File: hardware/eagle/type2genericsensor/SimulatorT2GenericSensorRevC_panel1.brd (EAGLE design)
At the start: 48.3 x 48.3 mm, 13 parts

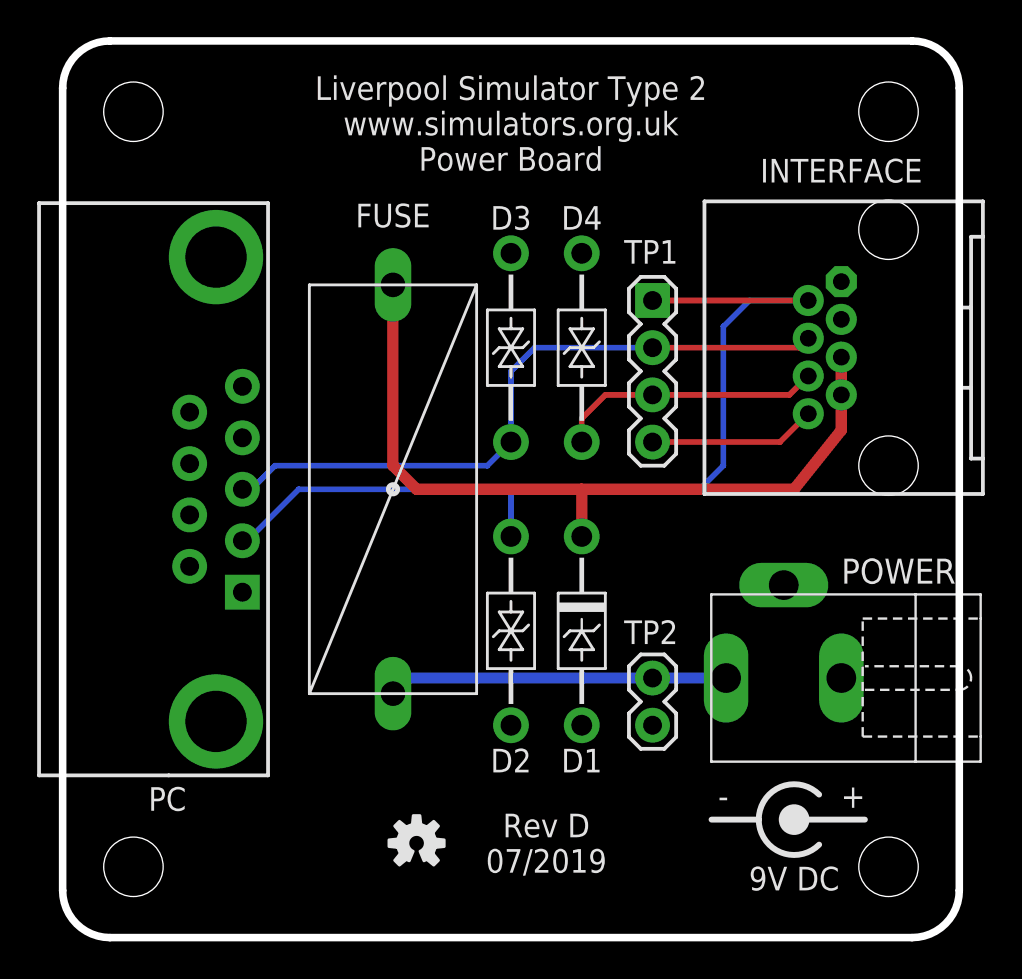
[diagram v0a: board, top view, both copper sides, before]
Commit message: Board Housekeeping
URL on silkscreens, caution messages, tidy up naming conventions.
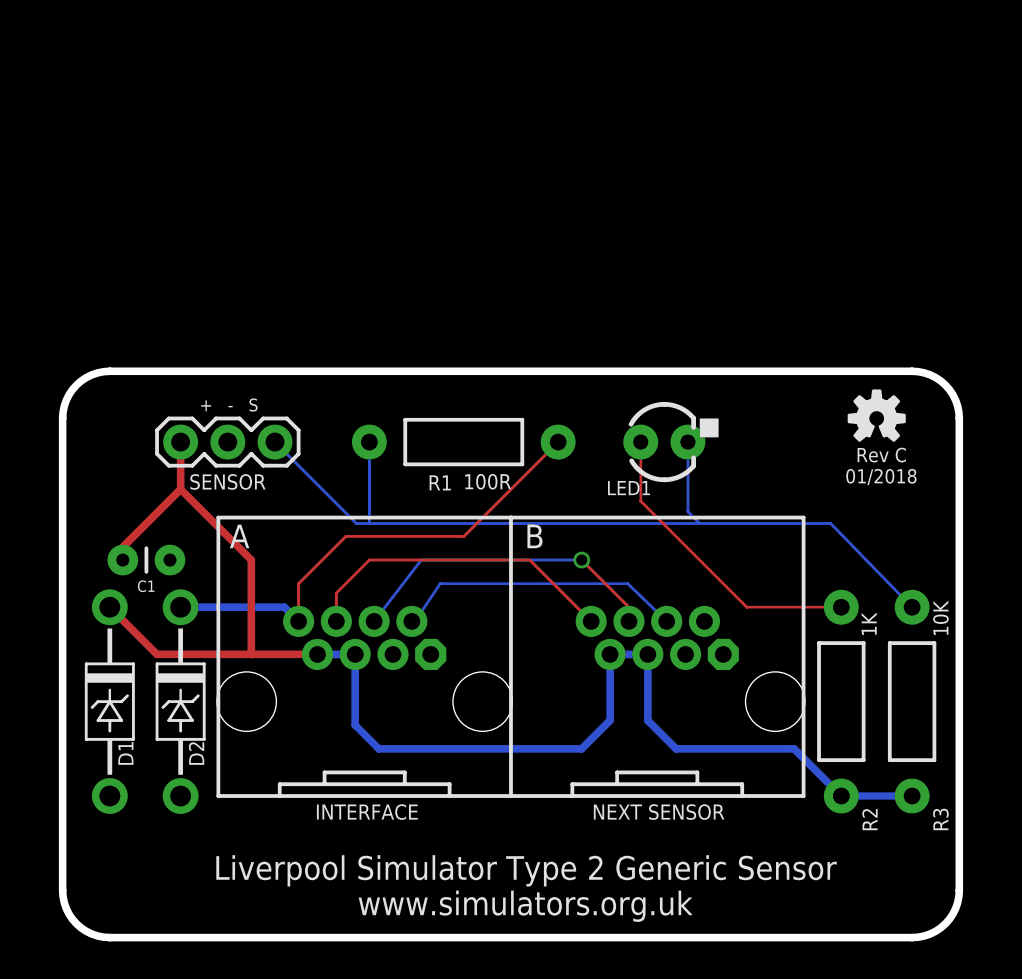
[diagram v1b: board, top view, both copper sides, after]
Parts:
- removed D3, D4: SA15CA, AIC_Custom:DO41_TVS_BI
- removed FUSE: 800mA, AIC_Custom:MCOMP-FUSE-HOLDER-PCB
- removed INTERFACE: RJ45-RJHSE-X08090DEG, AIC_Custom:RJ45-RJHSE-5080
- removed PC: (no value), AIC_Custom:MULTICOMP-DB9-FEMALE-PCB-90DEG
- removed POWER: 9V DC, AIC_Custom:CLIFF-FC681465P-DC-JACK
- removed TP1: (no value), SparkFun-Connectors:1X04
- removed TP2: (no value), SparkFun-Connectors:1X02
- removed U$1: (no value), AIC_Custom:CENTRE-POS-SILK
- removed U$2: (no value), AIC_Custom:WARNING_TRIANGLE_TPLACE
- added C1: 100nF, SparkFun-Passives:CAP-PTH-SMALL
- added E$1: (no value), AIC_Custom:WARNING_TRIANGLE_TPLACE
- added JP1: RJ45-RJHSE-5080-023HOLE, AIC_Custom:RJ45-RJHSE-5080-02-3HOLE
- added LED1: Blue, SparkFun-LED:LED3MM
- added R1: 100R, SparkFun-Passives:AXIAL-0.4
- added R2: 1K, SparkFun-Passives:AXIAL-0.4
- added R3: 10K, SparkFun-Passives:AXIAL-0.4
- added SENSOR: (no value), SparkFun-Connectors:1X03
- D1: value SA12A -> SA5.0A
- D2: value SA15CA -> SA5.0A; device AIC_Custom:DO41_TVS_BI -> AIC_Custom:DO41_TVS_UNI
- moved LOGO1 33.7 mm to (43.8, 27.9)
- moved D1 25.7 mm to (2.54, 12.7)
- moved D2 18.2 mm to (6.35, 12.7), turned to 90 degrees
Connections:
- removed net P8: INTERFACE.8, TP1.4
- removed net RXD: D3.C, INTERFACE.4, PC.3, TP1.2
- removed net TX2: D4.C, INTERFACE.6, TP1.3
- removed net TXD: D2.C, INTERFACE.2, PC.2, TP1.1
- removed net VIN: FUSE.2, POWER.1, TP2.1
- removed net VIN2: D1.CATHODE, FUSE.1, INTERFACE.5, INTERFACE.7
- new net !OUT!: D2.CATHODE, JP1.A8, R1.P$1
- new net B2: JP1.A6, JP1.B8
- new net B3: JP1.A4, JP1.B6
- new net B4: JP1.A2, JP1.B4
- new net LED: LED1.A, R2.P$1
- new net SIG: LED1.K, R1.P$2, R3.P$1, SENSOR.3
- new net VCC: C1.1, D1.CATHODE, JP1.A5, JP1.A7, JP1.B5, JP1.B7, R2.P$2, R3.P$2, SENSOR.1
- net GND: now also C1.2, D2.ANODE, JP1.A1, JP1.A3, JP1.B1, JP1.B3, SENSOR.2; no longer D2.A, D3.A, D4.A, INTERFACE.1, INTERFACE.3, PC.5, POWER.3, TP2.2
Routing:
- net VCC: track 0.00 -> 76.1 mm
- net TXD: track 51.1 -> 0.00 mm
- net SIG: track 0.00 -> 47.0 mm
- net VIN2: track 42.4 -> 0.00 mm
- net RXD: track 36.1 -> 0.00 mm
- net !OUT!: track 0.00 -> 26.0 mm
- net VIN: track 18.3 -> 0.00 mm
- net B2: track 0.00 -> 17.3 mm
- net B3: track 0.00 -> 17.2 mm, vias 0 -> 1
- net LED: track 0.00 -> 16.3 mm
- net B4: track 0.00 -> 15.6 mm
- net TX2: track 14.4 -> 0.00 mm
- net P8: track 9.01 -> 0.00 mm
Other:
- board size 48.3 x 48.3 mm -> 48.3 x 30.5 mm
- board text added: "+ - S"
- board text added: "C1"
- board text added: "D1"
- board text added: "D2"
- board text added: "INTERFACE"
- board text added: "LED1"
- board text added: "Liverpool Simulator Type 2 Generic Sensor www.simulators.org.uk"
- board text added: "NEXT SENSOR"
- board text added: "R1"
- board text added: "R2"
- board text added: "R3"
- board text added: "Rev C 01/2018"
- board text added: "SENSOR"
- board text removed: "Liverpool Simulator Type 2 www.simulators.org.uk Power Board"
- board text removed: "Rev D 07/2019"
